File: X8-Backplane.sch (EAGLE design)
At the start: 39 parts, among them U1 BD6221FSOP, U4 FQB27P06, U5 FQB27P06, U6 FQB27P06, U7 LM2678

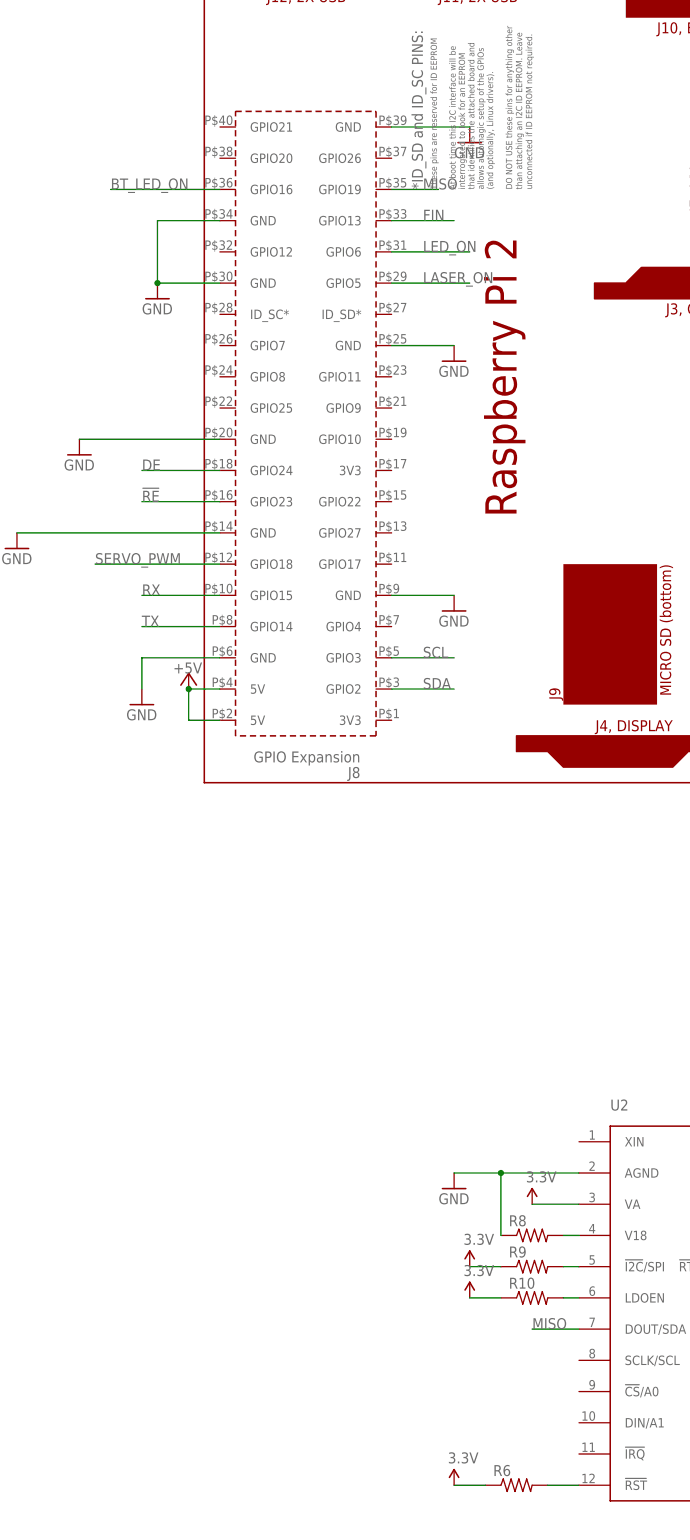
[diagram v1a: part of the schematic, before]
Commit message: Wired the spi to serial circuit
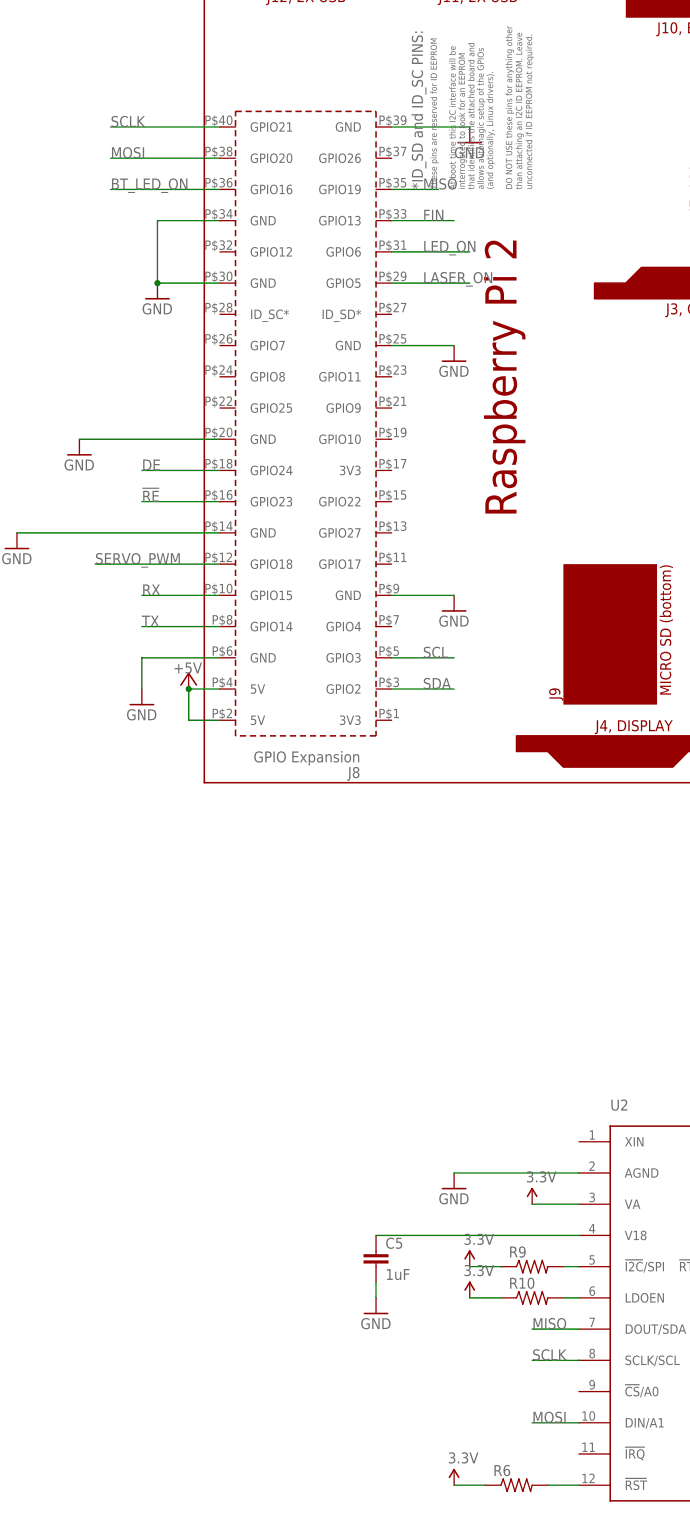
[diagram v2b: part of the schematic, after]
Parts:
- removed R8: (no value), SparkFun-Passives:RESISTOR0603-RES
- added C5: 1uF, SparkFun-Capacitors:0.1UF-25V(+80/-20%)(0603)
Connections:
- new net MOSI: PCB1.GPIO20, U2.DIN/A1
- new net SCLK: PCB1.GPIO21, U2.SCLK/SCL
- net GND: now also C5.2; no longer R8.1
- net N$9: now also C5.1; no longer R8.2
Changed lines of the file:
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@@
 <part name="GND23" library="supply1" deviceset="GND" device=""/>
 <part name="SUPPLY7" library="SparkFun-Aesthetics" deviceset="3.3V" device=""/>
-<part name="R8" library="SparkFun-Passives" deviceset="RESISTOR" device="0603-RES"/>
 <part name="SUPPLY8" library="SparkFun-Aesthetics" deviceset="3.3V" device=""/>
 <part name="R9" library="SparkFun-Passives" deviceset="RESISTOR" device="0603-RES"/>
@@
 <part name="SUPPLY10" library="SparkFun-Aesthetics" deviceset="3.3V" device=""/>
 <part name="R10" library="SparkFun-Passives" deviceset="RESISTOR" device="0603-RES"/>
+<part name="C5" library="SparkFun-Capacitors" deviceset="0.1UF-25V(+80/-20%)(0603)" device="" value="1uF"/>
+<part name="GND24" library="supply1" deviceset="GND" device=""/>
 </parts>
 <sheets>
@@
 <instance part="GND23" gate="1" x="157.48" y="-55.88"/>
 <instance part="SUPPLY7" gate="G$1" x="144.78" y="-30.48"/>
-<instance part="R8" gate="G$1" x="91.44" y="-40.64"/>
 <instance part="SUPPLY8" gate="G$1" x="91.44" y="-35.56"/>
 <instance part="R9" gate="G$1" x="91.44" y="-45.72"/>
@@
 <instance part="SUPPLY10" gate="G$1" x="81.28" y="-50.8"/>
 <instance part="R10" gate="G$1" x="91.44" y="-50.8"/>
+<instance part="C5" gate="G$1" x="66.04" y="-45.72"/>
+<instance part="GND24" gate="1" x="66.04" y="-53.34"/>
 </instances>
 <busses>
@@
 <pinref part="U2" gate="G$1" pin="AGND"/>
 <pinref part="GND20" gate="1" pin="GND"/>
-<wire x1="99.06" y1="-30.48" x2="86.36" y2="-30.48" width="0.1524" layer="91"/>
-<pinref part="R8" gate="G$1" pin="1"/>
-<wire x1="86.36" y1="-30.48" x2="78.74" y2="-30.48" width="0.1524" layer="91"/>
-<wire x1="86.36" y1="-40.64" x2="86.36" y2="-30.48" width="0.1524" layer="91"/>
-<junction x="86.36" y="-30.48"/>
+<wire x1="99.06" y1="-30.48" x2="78.74" y2="-30.48" width="0.1524" layer="91"/>
 </segment>
 <segment>
@@
 <wire x1="149.86" y1="-50.8" x2="157.48" y2="-50.8" width="0.1524" layer="91"/>
 <wire x1="157.48" y1="-50.8" x2="157.48" y2="-53.34" width="0.1524" layer="91"/>
+</segment>
+<segment>
+<pinref part="C5" gate="G$1" pin="2"/>
+<pinref part="GND24" gate="1" pin="GND"/>
+<wire x1="66.04" y1="-48.26" x2="66.04" y2="-50.8" width="0.1524" layer="91"/>
 </segment>
 </net>
@@
 </segment>
 </net>
-<net name="N$9" class="0">
-<segment>
-<pinref part="U2" gate="G$1" pin="V18"/>
-<pinref part="R8" gate="G$1" pin="2"/>
-<wire x1="99.06" y1="-40.64" x2="96.52" y2="-40.64" width="0.1524" layer="91"/>
-</segment>
-</net>
 <net name="N$10" class="0">
 <segment>
@@
 </segment>
 </net>
+<net name="N$9" class="0">
+<segment>
+<pinref part="C5" gate="G$1" pin="1"/>
+<pinref part="U2" gate="G$1" pin="V18"/>
+<wire x1="66.04" y1="-40.64" x2="99.06" y2="-40.64" width="0.1524" layer="91"/>
+</segment>
+</net>
+<net name="MOSI" class="0">
+<segment>
+<pinref part="U2" gate="G$1" pin="DIN/A1"/>
+<wire x1="99.06" y1="-71.12" x2="91.44" y2="-71.12" width="0.1524" layer="91"/>
+<label x="91.44" y="-71.12" size="1.778" layer="95"/>
+</segment>
+<segment>
+<pinref part="PCB1" gate="G$1" pin="GPIO20"/>
+<wire x1="40.64" y1="134.62" x2="22.86" y2="134.62" width="0.1524" layer="91"/>
+<label x="22.86" y="134.62" size="1.778" layer="95"/>
+</segment>
+</net>
+<net name="SCLK" class="0">
+<segment>
+<pinref part="U2" gate="G$1" pin="SCLK/SCL"/>
+<wire x1="99.06" y1="-60.96" x2="91.44" y2="-60.96" width="0.1524" layer="91"/>
+<label x="91.44" y="-60.96" size="1.778" layer="95"/>
+</segment>
+<segment>
+<pinref part="PCB1" gate="G$1" pin="GPIO21"/>
+<wire x1="40.64" y1="139.7" x2="22.86" y2="139.7" width="0.1524" layer="91"/>
+<label x="22.86" y="139.7" size="1.778" layer="95"/>
+</segment>
+</net>

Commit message: almost done reviewing the board
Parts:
- added C7, C8: 0.1u, SparkFun-Passives:CAP0603-CAP
- added J1: (no value), SparkFun-Connectors:M03PTH
- added J2: (no value), SparkFun-Connectors:M05PTH
- added J3: (no value), SparkFun-Connectors:M02PTH
- added J4: FEMALE 2x3, SparkFun-Connectors:M03X2FEMALE
- added R11, R8: (no value), SparkFun-Passives:RESISTOR0603-RES
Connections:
- removed net !RE: PCB1.GPIO23, U$1.!RE
- removed net DE: PCB1.GPIO24, U$1.DE
- net +12V: now also J4.1, J4.3, J4.5
- net +5V: now also J3.2
- net 3.3V: now also C7.1, C8.2, R11.2, R8.2, U$1.DE, U$4G$1.25
- net GND: now also C7.2, C8.1, J1.1, J2.1, J3.1, J4.2, J4.4, J4.6, U$1.!RE
- net MISO: now also J2.5
- net MOSI: now also J2.4
- net RX_BT: now also J2.3
- net SCL: now also J1.2, R8.1
- net SDA: now also J1.3, R11.1
- net TX_BT: now also J2.2
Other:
- note added: "data pins"
- note added: "debugging pins"
- note added: "power pins"

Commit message: Fixed routing issues
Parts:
- removed J4: FEMALE 2x3, SparkFun-Connectors:M03X2FEMALE
- added LED6, LED7, LED8: (no value), led:LEDSML0603
- added R12, R13, R14: 330, resistor:R-US_R0603
- added SV1, SV2: (no value), con-lstb:MA03-1
- added V+_ESC1, V+_ESC5: (no value), SparkFun-Connectors:BANANA_CONN
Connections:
- new net LED1: PCB1.GPIO7, R12.2
- new net LED2: PCB1.GPIO8, R13.2
- new net LED3: PCB1.GPIO25, R14.2
- new net N$13: LED6.A, R12.1
- new net N$14: LED7.A, R13.1
- new net N$15: LED8.A, R14.1
- new net RESET: PCB1.GPIO4, U$3.RST
- net +12V: now also SV1.1, SV1.2, SV1.3, U$4G$2.12V, V+_ESC5.1; no longer J4.1, J4.3, J4.5, U$4G$2.29
- net DSCLM: now also U$4G$1.SDA_DIFF_H; no longer U$4G$1.35
- net DSCLP: now also U$4G$1.35; no longer U$4G$1.36
- net DSDAM: now also U$4G$1.SCL; no longer U$4G$1.37
- net DSDAP: now also U$4G$1.37; no longer U$4G$1.38
- net GND: now also LED6.C, LED7.C, LED8.C, SV2.1, SV2.2, SV2.3, V+_ESC1.1; no longer J4.2, J4.4, J4.6
- net RX_BT: now also U$4G$1.GND_PIEZO_1; no longer U$4G$1.21
- net RX_H: now also U$4G$1.SCL_DIFF_L; no longer U$4G$1.29
- net RX_L: now also U$4G$1.28; no longer U$4G$1.27
- net SCL: now also U$4G$1.39; no longer U$4G$1.40
- net SDA: now also U$4G$1.SDA; no longer U$4G$1.39
- net SERVO_PWM: now also U$4G$1.33; no longer U$4G$1.34
- net TX_BT: now also U$4G$1.24; no longer U$4G$1.23
- net TX_H: now also U$4G$1.SDA_DIFF_L; no longer U$4G$1.33
- net TX_L: now also U$4G$1.SCL_DIFF_H; no longer U$4G$1.31

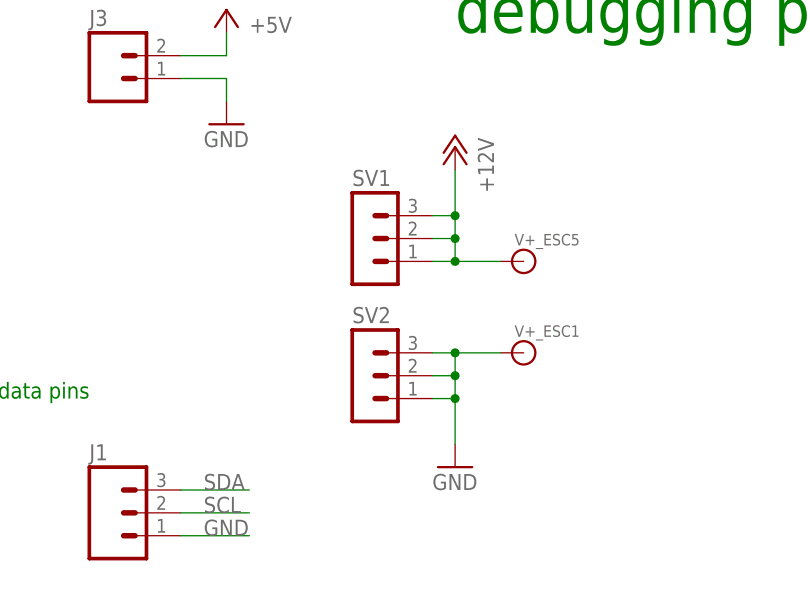
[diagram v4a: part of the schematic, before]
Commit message: cleaned up gnd plane and added labels
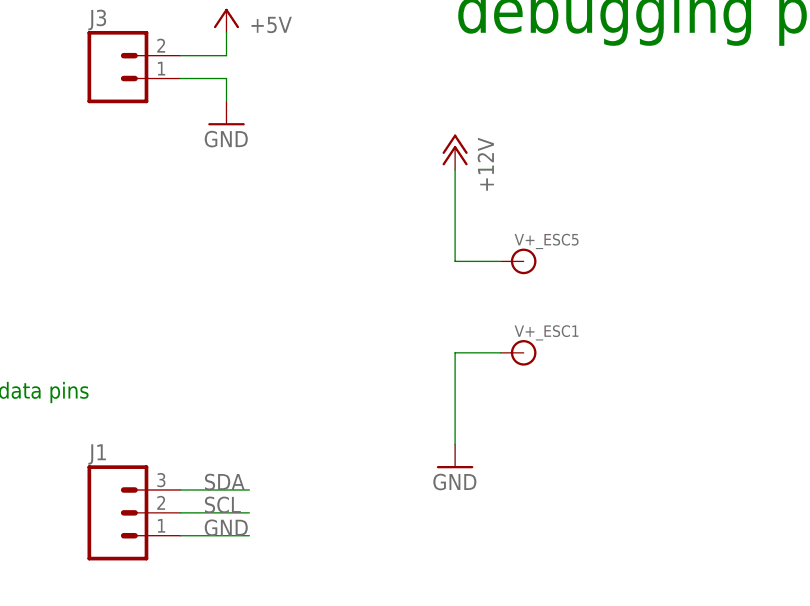
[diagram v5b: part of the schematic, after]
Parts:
- removed SV1, SV2: (no value), con-lstb:MA03-1
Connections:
- net +12V: no longer SV1.1, SV1.2, SV1.3
- net GND: no longer SV2.1, SV2.2, SV2.3
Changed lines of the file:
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@@
 <part name="R14" library="resistor" deviceset="R-US_" device="R0603" value="330"/>
 <part name="GND33" library="SparkFun-Aesthetics" deviceset="GND" device=""/>
-<part name="SV1" library="con-lstb" deviceset="MA03-1" device=""/>
-<part name="SV2" library="con-lstb" deviceset="MA03-1" device=""/>
 <part name="P+10" library="supply1" deviceset="+12V" device=""/>
 <part name="GND34" library="SparkFun-Aesthetics" deviceset="GND" device=""/>
@@
 <instance part="R14" gate="G$1" x="203.2" y="190.5" rot="R90"/>
 <instance part="GND33" gate="1" x="203.2" y="165.1"/>
-<instance part="SV1" gate="G$1" x="340.36" y="-38.1"/>
-<instance part="SV2" gate="G$1" x="340.36" y="-53.34"/>
 <instance part="P+10" gate="1" x="350.52" y="-27.94" rot="MR0"/>
 <instance part="GND34" gate="1" x="350.52" y="-63.5"/>
@@
 </segment>
 <segment>
-<pinref part="SV2" gate="G$1" pin="1"/>
 <pinref part="GND34" gate="1" pin="GND"/>
-<wire x1="347.98" y1="-55.88" x2="350.52" y2="-55.88" width="0.1524" layer="91"/>
-<wire x1="350.52" y1="-55.88" x2="350.52" y2="-60.96" width="0.1524" layer="91"/>
-<pinref part="SV2" gate="G$1" pin="2"/>
-<wire x1="347.98" y1="-53.34" x2="350.52" y2="-53.34" width="0.1524" layer="91"/>
-<wire x1="350.52" y1="-53.34" x2="350.52" y2="-55.88" width="0.1524" layer="91"/>
-<junction x="350.52" y="-55.88"/>
-<pinref part="SV2" gate="G$1" pin="3"/>
-<wire x1="347.98" y1="-50.8" x2="350.52" y2="-50.8" width="0.1524" layer="91"/>
-<wire x1="350.52" y1="-50.8" x2="350.52" y2="-53.34" width="0.1524" layer="91"/>
-<junction x="350.52" y="-53.34"/>
+<wire x1="350.52" y1="-50.8" x2="350.52" y2="-60.96" width="0.1524" layer="91"/>
 <pinref part="V+_ESC1" gate="G$1" pin="1"/>
 <wire x1="350.52" y1="-50.8" x2="355.6" y2="-50.8" width="0.1524" layer="91"/>
-<junction x="350.52" y="-50.8"/>
 </segment>
 </net>
@@
 </segment>
 <segment>
-<pinref part="SV1" gate="G$1" pin="3"/>
 <pinref part="P+10" gate="1" pin="+12V"/>
-<wire x1="347.98" y1="-35.56" x2="350.52" y2="-35.56" width="0.1524" layer="91"/>
-<wire x1="350.52" y1="-35.56" x2="350.52" y2="-30.48" width="0.1524" layer="91"/>
-<pinref part="SV1" gate="G$1" pin="2"/>
-<wire x1="347.98" y1="-38.1" x2="350.52" y2="-38.1" width="0.1524" layer="91"/>
-<wire x1="350.52" y1="-38.1" x2="350.52" y2="-35.56" width="0.1524" layer="91"/>
-<junction x="350.52" y="-35.56"/>
-<pinref part="SV1" gate="G$1" pin="1"/>
-<wire x1="347.98" y1="-40.64" x2="350.52" y2="-40.64" width="0.1524" layer="91"/>
-<wire x1="350.52" y1="-40.64" x2="350.52" y2="-38.1" width="0.1524" layer="91"/>
-<junction x="350.52" y="-38.1"/>
+<wire x1="350.52" y1="-40.64" x2="350.52" y2="-30.48" width="0.1524" layer="91"/>
 <pinref part="V+_ESC5" gate="G$1" pin="1"/>
 <wire x1="350.52" y1="-40.64" x2="355.6" y2="-40.64" width="0.1524" layer="91"/>
-<junction x="350.52" y="-40.64"/>
 </segment>
 </net>
